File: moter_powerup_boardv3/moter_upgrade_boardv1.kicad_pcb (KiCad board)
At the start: 2 copper layers, 36 parts, among them J1 Conn_01x05_Socket, J2 Conn_ST_STDC14, J3 Conn_01x02_Socket, J4 Conn_01x02_Socket, J5 Conn_01x02_Socket, J6 Conn_01x03_Pin, Q2 Q_PMOS_GDS, SW1 SW_Wuerth_450301014042, SW2 SW_Push, SW3 SW_Push, SW4 SW_Push, U2 PTCAN3414DDFR, U3 STM32H533CETx

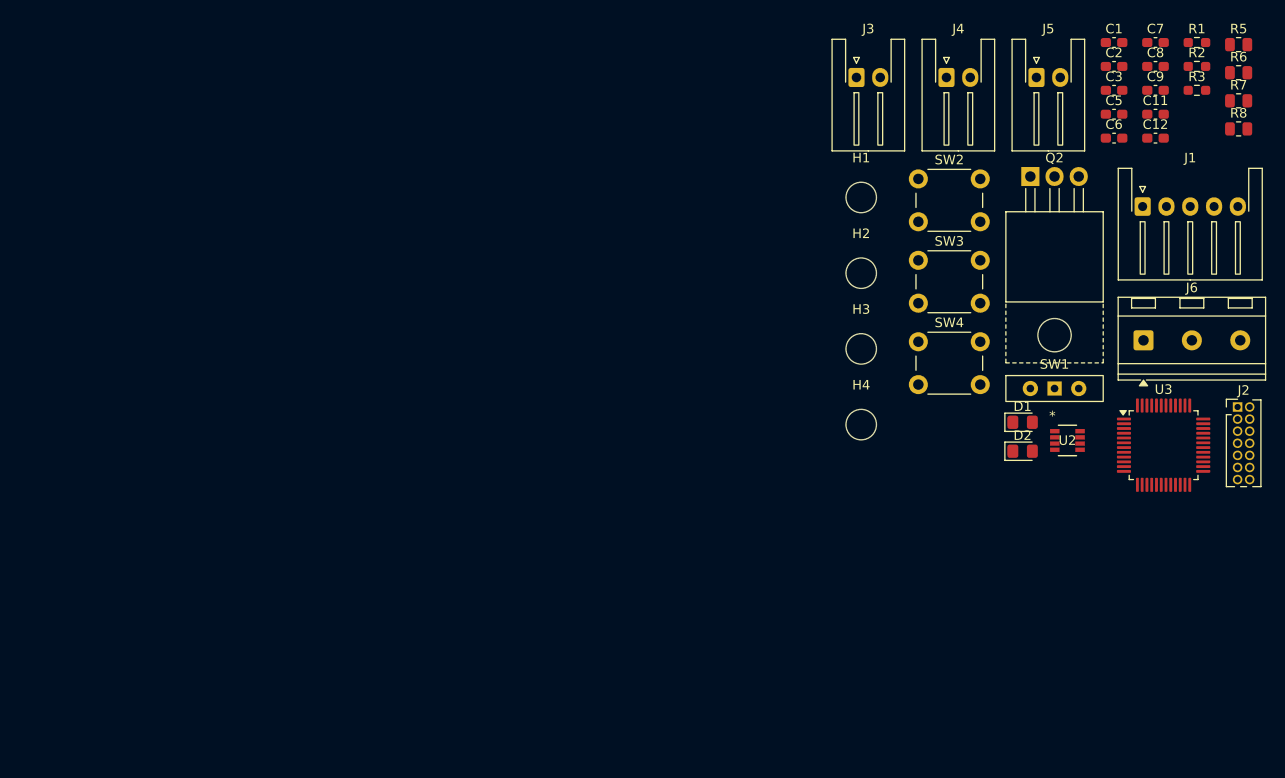
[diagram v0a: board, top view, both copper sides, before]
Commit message: MDPID基板を作ったりLED基板の電源回りをいじった
MDPIDの電源変更+配線
LED基板の電源変更(未配線)
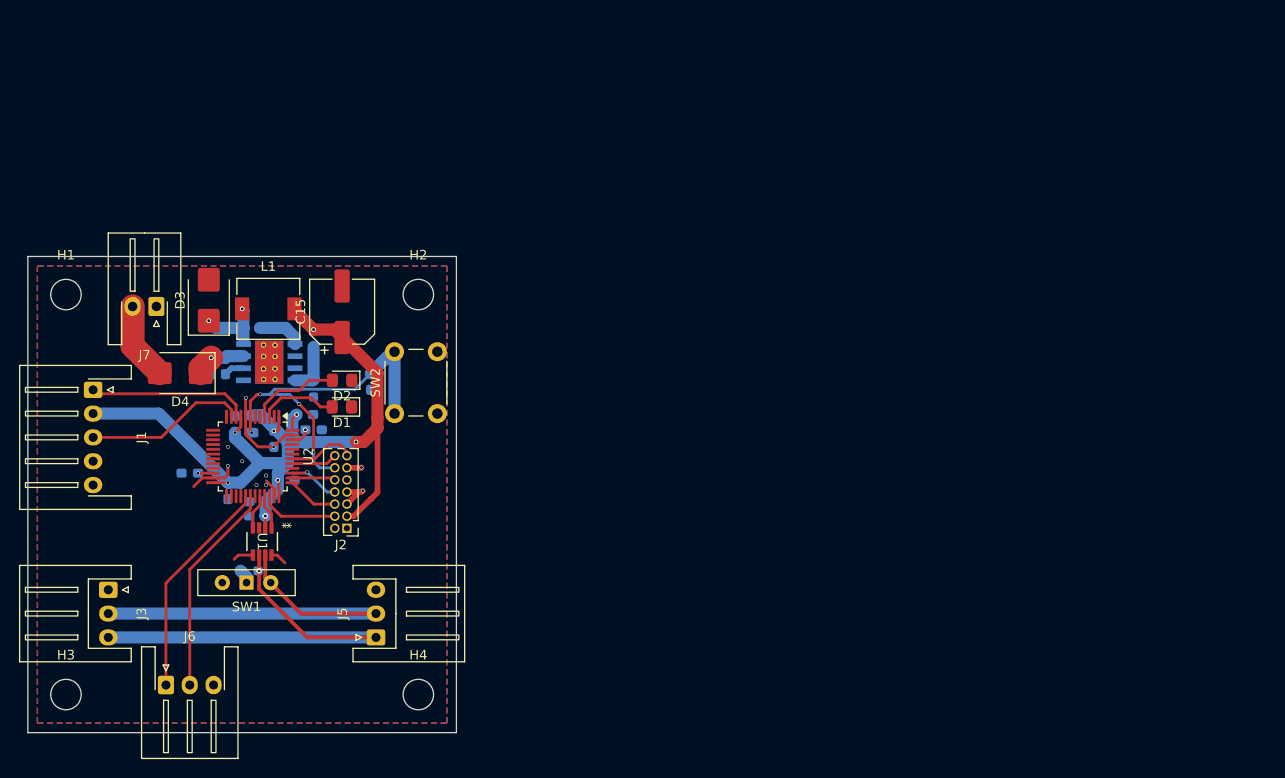
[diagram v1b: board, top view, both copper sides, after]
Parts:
- removed J4: Conn_01x02_Socket, Connector_JST:JST_XH_S2B-XH-A-1_1x02_P2.50mm_Horizontal
- removed Q2: Q_PMOS_GDS, Package_TO_SOT_THT:TO-220-3_Horizontal_TabUp
- removed R2: 1k, Resistor_SMD:R_0603_1608Metric_Pad0.98x0.95mm_HandSolder
- removed R8: 100k, Resistor_SMD:R_0805_2012Metric
- removed SW3, SW4: SW_Push, Button_Switch_THT:SW_PUSH_6mm
- added C10: 0.1uF, Capacitor_SMD:C_0603_1608Metric_Pad1.08x0.95mm_HandSolder, B.Cu at (79.1, 76.6)
- added C14: 4.7uF, Capacitor_SMD:C_0603_1608Metric_Pad1.08x0.95mm_HandSolder, B.Cu at (70.8, 71.5)
- added C15: 220uF, Capacitor_SMD:CP_Elec_6.3x4.5, F.Cu at (83.0, 65.8)
- added C4: 2.2uF, Capacitor_SMD:C_0603_1608Metric_Pad1.08x0.95mm_HandSolder, B.Cu at (67.0, 82.8)
- added D3: D_Shockley, Diode_SMD:D_SMB, F.Cu at (69.0, 64.6)
- added D4: D_Shockley, Diode_SMD:D_SMB, F.Cu at (66.0, 72.2)
- added J7: Conn_01x02_Socket, Connector_JST:JST_XH_S2B-XH-A-1_1x02_P2.50mm_Horizontal, F.Cu at (63.5, 65.2)
- added L1: 22uH, Inductor_SMD:L_6.3x6.3_H3, F.Cu at (75.2, 65.5)
- added R4: 1k, Resistor_SMD:R_0603_1608Metric_Pad0.98x0.95mm_HandSolder, B.Cu at (83.0, 75.8)
- added U1: PTCAN3414DDFR, 26off_tcan3414ddfr:SOT-23-THIN-8_DDF_TEX-M, F.Cu at (74.6, 89.9)
- C1: value 0.1uF -> 4.7uF; moved to B.Cu
- C11: value 2.2uF -> 4.7uF; moved to B.Cu
- C12: value 2.2uF -> 10nF; moved to B.Cu
- C2, C6, C8, C9, R1: moved to B.Cu
- C3: value 0.1uF -> 0.1uf; moved to B.Cu
- C5: value 0.1uf -> 2.2uF; moved to B.Cu
- C7: value 4.7uF -> 0.1uF; moved to B.Cu
- J3, J5: value Conn_01x02_Socket -> Conn_01x03_Pin; footprint Connector_JST:JST_XH_S2B-XH-A-1_1x02_P2.50mm_Horizontal -> Connector_JST:JST_XH_S3B-XH-A_1x03_P2.50mm_Horizontal
- J6: footprint TerminalBlock_RND:TerminalBlock_RND_205-00233_1x03_P5.08mm_Horizontal -> Connector_JST:JST_XH_S3B-XH-A-1_1x03_P2.50mm_Horizontal
- R3: value 1k -> 10k; footprint Resistor_SMD:R_0603_1608Metric_Pad0.98x0.95mm_HandSolder -> Resistor_SMD:R_0805_2012Metric; moved to B.Cu
- R5: value 10k -> 1k; footprint Resistor_SMD:R_0805_2012Metric -> Resistor_SMD:R_0603_1608Metric_Pad0.98x0.95mm_HandSolder; moved to B.Cu
- R6: footprint Resistor_SMD:R_0805_2012Metric -> Resistor_SMD:R_0603_1608Metric_Pad0.98x0.95mm_HandSolder; moved to B.Cu
- R7: value 10k -> 5.90k; footprint Resistor_SMD:R_0805_2012Metric -> Resistor_SMD:R_0603_1608Metric_Pad0.98x0.95mm_HandSolder; moved to B.Cu
- U2: value PTCAN3414DDFR -> STM32H533CETx; footprint 26off_tcan3414ddfr:SOT-23-THIN-8_DDF_TEX -> Package_QFP:LQFP-48_7x7mm_P0.5mm
- U3: value STM32H533CETx -> TPS5430DDA; footprint Package_QFP:LQFP-48_7x7mm_P0.5mm -> Package_SO:TI_SO-PowerPAD-8_ThermalVias; moved to B.Cu
- moved R1 113.9 mm to (73.2, 93.0), turned to 180 degrees
- moved J1 111.9 mm to (56.9, 74.0), turned to -90 degrees
- moved J6 108.8 mm to (64.5, 105.0)
- moved C8 107.1 mm to (71.0, 84.6), turned to -90 degrees
- moved R3 105.3 mm to (73.5, 77.6), turned to -90 degrees
- moved C7 104.6 mm to (71.8, 77.6), turned to 90 degrees
- moved C11 102.6 mm to (69.2, 71.5), turned to -90 degrees
- moved C1 102.1 mm to (74.1, 85.8)
- moved R7 101.7 mm to (80.0, 73.8), turned to -90 degrees
- moved C2 101.6 mm to (74.1, 87.2)
- moved R6 101.1 mm to (80.0, 68.6), turned to -90 degrees
- moved R5 100.5 mm to (83.0, 73.0)
- moved C9 100.0 mm to (77.1, 83.5)
- moved C12 97.0 mm to (73.5, 67.5), turned to 180 degrees
- moved J3 95.2 mm to (58.4, 95.0), turned to -90 degrees
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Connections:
- C1 pad 1: +3.3V -> GND
- C1 pad 2: GND -> +3.3V
- C11 pad 1: Net-(C11-Pad1) -> +24V
- C12 pad 1: Net-(C12-Pad1) -> Net-(U3-BOOT)
- C12 pad 2: GND -> Net-(D3-K)
- C2 pad 1: +3.3V -> GND
- C2 pad 2: GND -> +3.3V
- C3 pad 1: +3.3V -> nrst
- C5 pad 1: nrst -> Net-(C5-Pad1)
- C6 pad 1: GND -> +3.3V
- C6 pad 2: +3.3V -> GND
- C7 pad 1: GND -> +3.3V
- C7 pad 2: +3.3V -> GND
- J1 pad 1: en-b -> en-a
- J1 pad 3: en-a -> en-b
- J3 pad 1: CAN1_+ -> GND
- J3 pad 2: CAN1_- -> CAN1_+
- J5 pad 1: GND -> CAN1_-
- J5 pad 2: Net-(J5-Pin_2) -> CAN1_+
- J6 pad 1: dir to moter -> PWM1
- J6 pad 2: pwm to moter -> PWM2
- R3 pad 1: GND -> +3.3V
- R3 pad 2: Net-(D2-K) -> nrst
- R5 pad 1: +3.3V -> GND
- R5 pad 2: /mb -> Net-(D2-K)
- R6 pad 2: nrst -> Net-(U3-VSENSE)
- R7 pad 1: +3.3V -> Net-(U3-VSENSE)
- R7 pad 2: /ma -> GND
- SW1 pad 1: CAN1_- -> CAN1R
- SW1 pad 2: CAN1R -> CAN1_+
- SW2 pad 1: /ma -> nrst
- U2 pad 1: CAN1tx -> +3.3V
- U2 pad 2: +3.3V -> unconnected-(U2-PC13-Pad2)
- U2 pad 3: GND -> Net-(D1-A)
- U2 pad 4: CAN1rx -> Net-(D2-A)
- U2 pad 5: GND -> /ma
- U2 pad 6: CAN1_- -> unconnected-(U2-PH1-Pad6)
- U2 pad 7: CAN1_+ -> nrst
- U3 pad 1: +3.3V -> Net-(U3-BOOT)
- U3 pad 3: /mb -> unconnected-(U3-NC-Pad3)
- U3 pad 4: Net-(D2-A) -> Net-(U3-VSENSE)
- U3 pad 5: /ma -> unconnected-(U3-EN-Pad5)
- U3 pad 6: Net-(D1-A) -> GND
- U3 pad 7: nrst -> +24V
- U3 pad 8: GND -> Net-(D3-K)
- U3 pad 9: unconnected-(U3-VDDA-Pad9) -> GND
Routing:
- net +3.3V: track 0.00 -> 94.3 mm, vias 0 -> 8
- net CAN1_-: track 0.00 -> 46.2 mm, vias 0 -> 1
- net CAN1_+: track 0.00 -> 43.7 mm
- net nrst: track 0.00 -> 39.9 mm, vias 0 -> 4
- net GND: track 0.00 -> 28.0 mm, vias 0 -> 10
- net PWM1: track 0.00 -> 23.3 mm
- net PWM2: track 0.00 -> 22.5 mm
- net en-b: track 0.00 -> 17.1 mm
- net en-a: track 0.00 -> 16.9 mm
- net Net-(D2-A): track 0.00 -> 9.46 mm
- net Net-(D1-A): track 0.00 -> 8.26 mm
- net swdio: track 0.00 -> 8.26 mm
- net Net-(D4-A): track 0.00 -> 8.18 mm
- net Net-(D3-K): track 0.00 -> 7.37 mm, vias 0 -> 2
- net strx: track 0.00 -> 7.08 mm
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- added copper zone on B.Cu, net GND
- added copper zone on F.Cu, net GND
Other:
- board outline added: 45 x 50 mm
